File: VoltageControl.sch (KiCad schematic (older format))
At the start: 10 parts, among them U201 LMV358

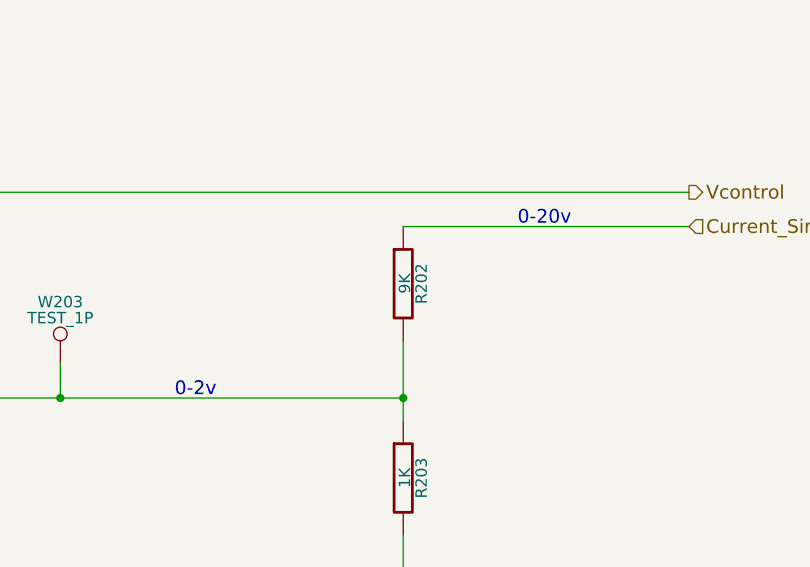
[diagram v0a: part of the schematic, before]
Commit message: revised resistors to match available values, replaced FET (old FET was obsolete/unavail)
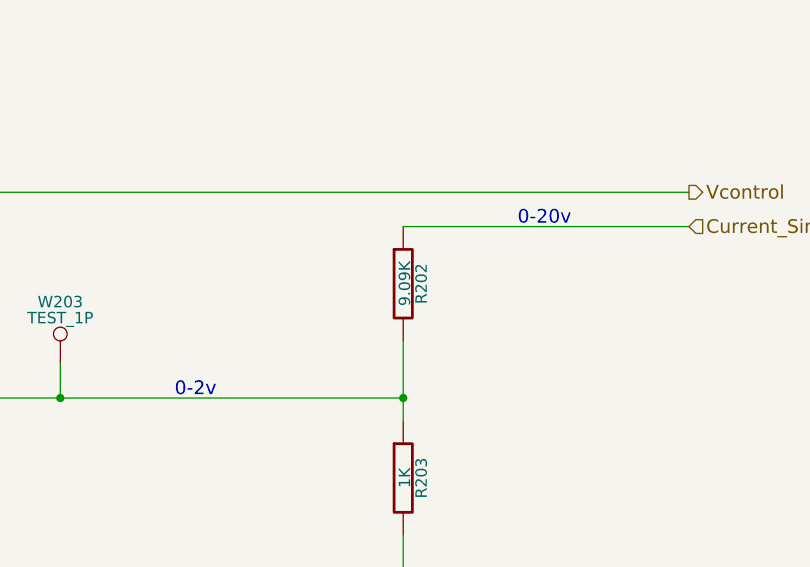
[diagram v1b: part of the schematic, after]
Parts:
- R202: value 9K -> 9.09K
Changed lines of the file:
@@
 $EndComp
 $Comp
-L GND #PWR202
+L GND #PWR03
 U 1 1 54DB1D11
 P 5750 3600
-F 0 "#PWR202" H 5750 3350 60  0001 C CNN
+F 0 "#PWR03" H 5750 3350 60  0001 C CNN
 F 1 "GND" H 5750 3450 60  0000 C CNN
 F 2 "" H 5750 3600 60  0000 C CNN
@@
 	5750 1950 5750 2650
 $Comp
-L GND #PWR201
+L GND #PWR04
 U 1 1 54DB1D2C
 P 5150 2650
-F 0 "#PWR201" H 5150 2400 60  0001 C CNN
+F 0 "#PWR04" H 5150 2400 60  0001 C CNN
 F 1 "GND" H 5150 2500 60  0000 C CNN
 F 2 "" H 5150 2650 60  0000 C CNN
@@
 P 8700 3450
 F 0 "R202" V 8780 3450 50  0000 C CNN
-F 1 "9K" V 8707 3451 50  0000 C CNN
+F 1 "9.09K" V 8707 3451 50  0000 C CNN
 F 2 "Resistors_SMD:R_0805" V 8630 3450 30  0001 C CNN
 F 3 "" H 8700 3450 30  0000 C CNN
